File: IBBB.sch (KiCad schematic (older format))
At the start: 11 parts

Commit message: Updates to schematics.  Still very rough
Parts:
- removed C?: 0.1u, symbol C
- removed IC?: AT24CS32-STUM, SOT-23-5, symbol AT24CS32-STUM
- removed R? (x2): 1.5k, 1%, symbol R
- removed R?: 10k, 1%, symbol R
- removed U?: OSD3358, symbol OSD3358
- added C?: 2.2u, symbol C
- added R?: 10k, symbol R
- added SW?: SW_PUSH, symbol SW_PUSH
- added U?: SN74LVC1G07, symbol SN74LVC1G07
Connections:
- net +3V3_B: now also R?.1
- net GND: now also C?.2, SW?.1, U?.3
- net at U?.A10 (WARMRSTN): now also C?.1, R?.2, SW?.2, U?.4 (Y)
- net at U?.A19 (PMIC_OUT_NWAKEUP): now also U?.C5 (EXT_WAKEUP)
- net at U?.A20 (PMIC_OUT_PGOOD): now also U?.B15 (PWRONRSTN), U?.2 (A)
- net at U?.B18 (EXTINTN): now also U?.B19 (PMIC_OUT_NINT)
- net at U?.B20 (PMIC_OUT_LDO_PGOOD): now also U?.B5 (RTC_PWRONRSTN)
- net USB_DC: now reaches U?.Y8 (VIN_USB_Y8)
- net USB_DC: now also U?.Y9 (VIN_USB_Y9)
- net I2C0_SCA renamed USB_UART/I2C0_SDA
- net I2C0_SCL renamed USB_UART/I2C0_SCL
- new net VDD_RTC: U?.5
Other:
- note added: "POWER"
- note added: "RESET"
- note removed: "Board ID"
- moved on the sheet: CON?, D?, R?, SW?, U?A

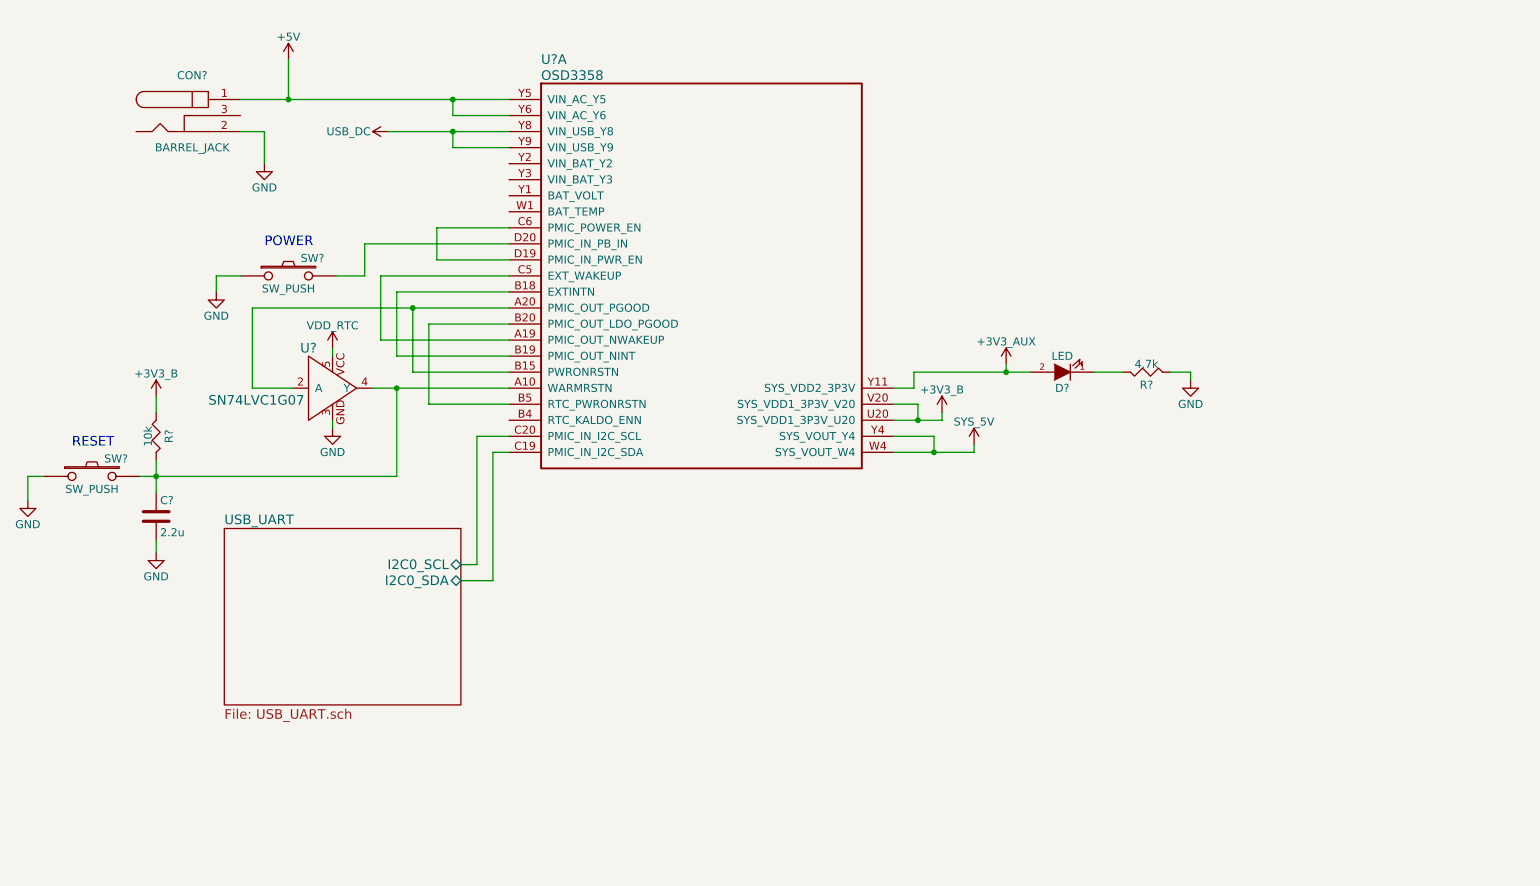
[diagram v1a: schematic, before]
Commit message: Added oscillator and power sheets
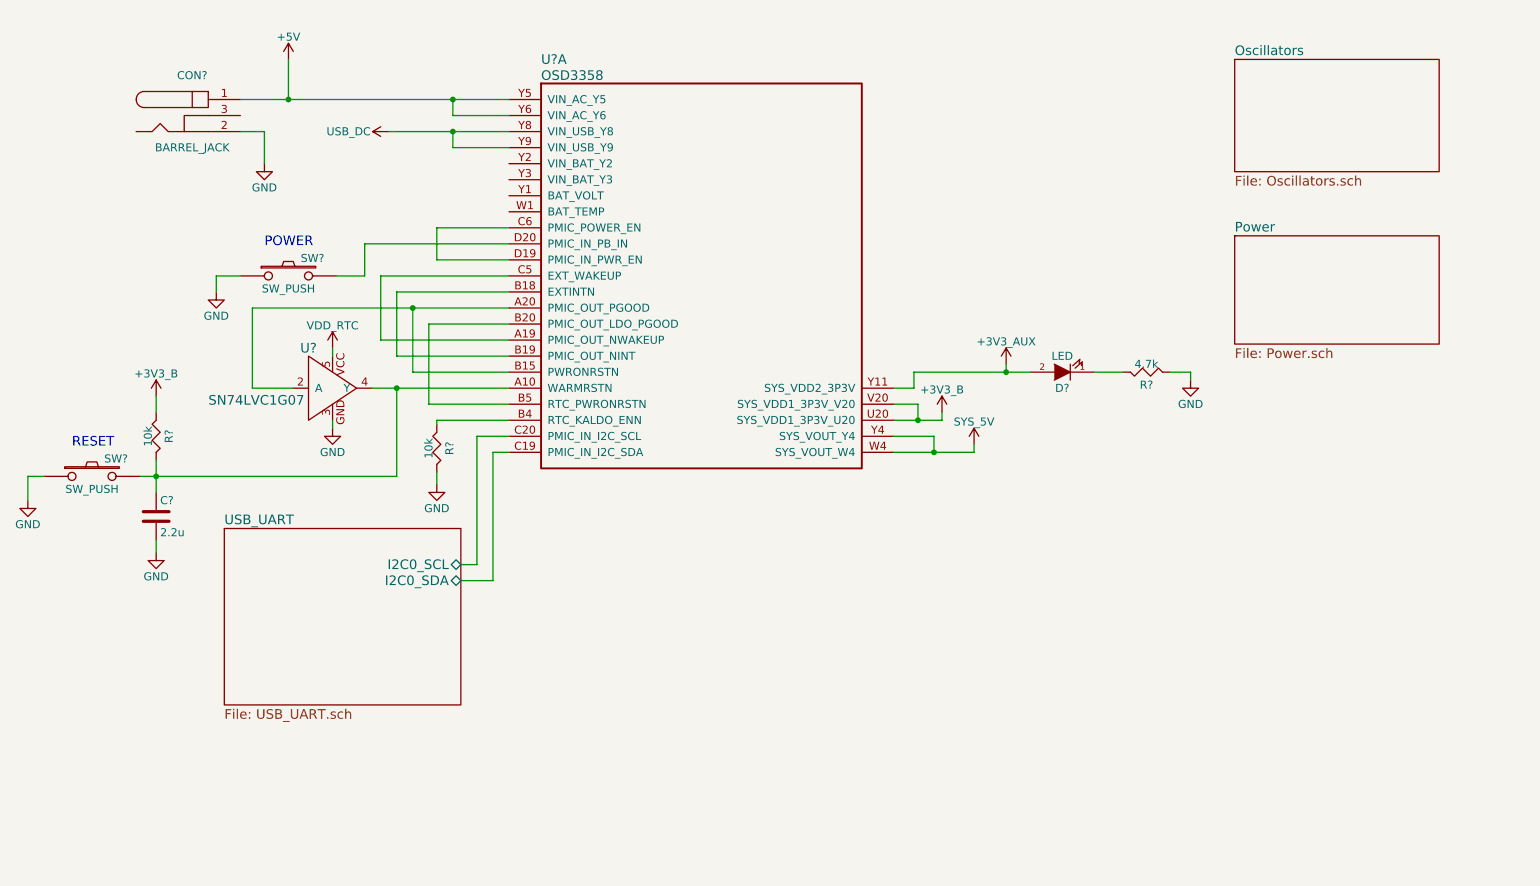
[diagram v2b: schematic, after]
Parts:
- added R?: 10k, symbol R
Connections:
- net GND: now also R?.2
- net at U?.B4 (RTC_KALDO_ENN): now also R?.1
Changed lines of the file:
@@
 $Descr A4 11693 8268
 encoding utf-8
-Sheet 1 2
+Sheet 1 4
 Title "IBBB"
 Date "2016-05-14"
@@
 $EndComp
 Wire Wire Line
-	2325 1200 2625 1200
-Wire Wire Line
-	2625 1200 3650 1200
-Wire Wire Line
-	3650 1200 4000 1200
+	2325 1200 4000 1200
 Wire Wire Line
 	4000 1300 3650 1300
@@
 $EndComp
 Wire Wire Line
-	6400 3400 6650 3400
-Wire Wire Line
-	6650 3400 6900 3400
+	6400 3400 6900 3400
 Wire Wire Line
 	6400 3300 6650 3300
@@
 	6550 3100 6550 3200
 Wire Wire Line
-	6400 3200 6550 3200
-Wire Wire Line
-	6550 3200 6700 3200
+	6400 3200 6700 3200
 Wire Wire Line
 	6700 3200 6700 3150
@@
 	6525 3000 6525 2900
 Wire Wire Line
-	6525 2900 7100 2900
-Wire Wire Line
-	7100 2900 7250 2900
+	6525 2900 7250 2900
 Wire Wire Line
 	7100 2900 7100 2850
@@
 $EndComp
 Wire Wire Line
-	2400 2500 3400 2500
-Wire Wire Line
-	3400 2500 4000 2500
+	2400 2500 4000 2500
 Wire Wire Line
 	3400 2500 3400 2900
@@
 Connection ~ 3400 2500
 Wire Wire Line
-	3150 3000 3300 3000
-Wire Wire Line
-	3300 3000 4000 3000
+	3150 3000 4000 3000
 Wire Wire Line
 	2900 3250 2900 3200
@@
 $EndComp
 Wire Wire Line
-	1800 3450 1800 3550
-Wire Wire Line
-	1800 3550 1800 3650
-Wire Wire Line
-	1700 3550 1800 3550
-Wire Wire Line
-	1800 3550 3300 3550
+	1800 3450 1800 3650
+Wire Wire Line
+	1700 3550 3300 3550
 Connection ~ 1800 3550
 Wire Wire Line
@@
 	3900 4200 3700 4200
 Wire Wire Line
-	3250 1400 3650 1400
-Wire Wire Line
-	3650 1400 4000 1400
+	3250 1400 4000 1400
 Wire Wire Line
 	4000 1500 3650 1500
@@
 	0    -1   -1   0
 $EndComp
+$Sheet
+S 8525 950  1275 700
+U 5738A7C2
+F0 "Oscillators" 60
+F1 "Oscillators.sch" 60
+$EndSheet
+$Sheet
+S 8525 2050 1275 675
+U 5738C205
+F0 "Power" 60
+F1 "Power.sch" 60
+$EndSheet
+$Comp
+L R R?
+U 1 1 5738D8EE
+P 3550 3375
+F 0 "R?" V 3630 3375 50  0000 C CNN
+F 1 "10k" V 3500 3375 50  0000 C CNN
+F 2 "" V 3480 3375 30  0000 C CNN
+F 3 "" H 3550 3375 30  0000 C CNN
+	1    3550 3375
+	1    0    0    -1
+$EndComp
+Wire Wire Line
+	4000 3200 3550 3200
+Wire Wire Line
+	3550 3200 3550 3225
+$Comp
+L GND #PWR?
+U 1 1 5738D9A2
+P 3550 3600
+F 0 "#PWR?" H 3550 3350 50  0001 C CNN
+F 1 "GND" H 3550 3450 50  0000 C CNN
+F 2 "" H 3550 3600 50  0000 C CNN
+F 3 "" H 3550 3600 50  0000 C CNN
+	1    3550 3600
+	1    0    0    -1
+$EndComp
+Wire Wire Line
+	3550 3600 3550 3525
 $EndSCHEMATC

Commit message: Added analog and GPIO sheet
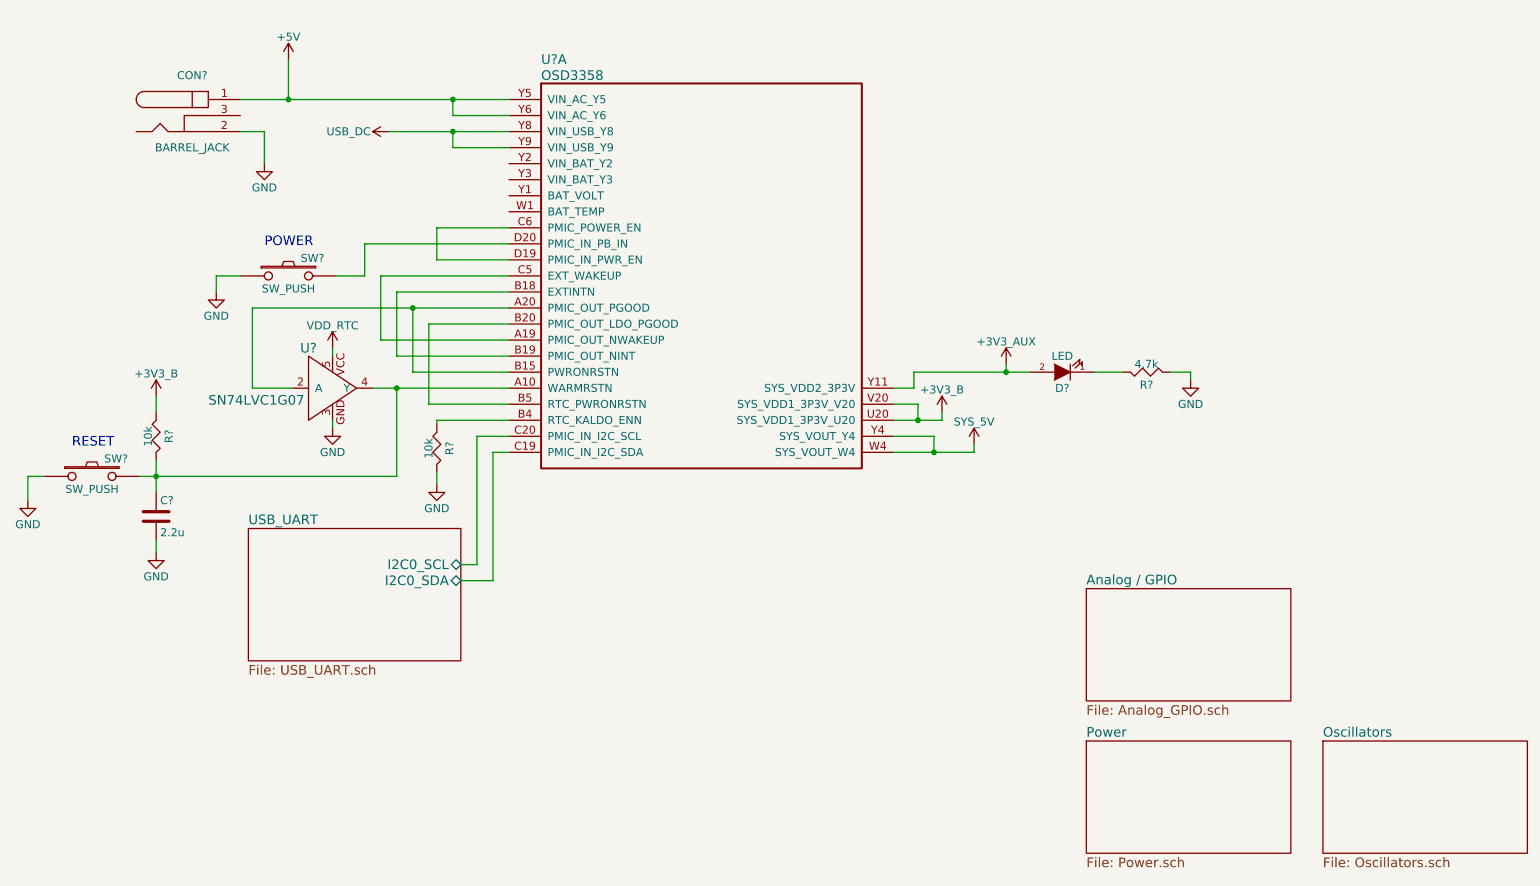
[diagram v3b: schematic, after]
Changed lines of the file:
@@
 $Descr A4 11693 8268
 encoding utf-8
-Sheet 1 4
+Sheet 1 5
 Title "IBBB"
 Date "2016-05-14"
@@
 $EndComp
 $Sheet
-S 2225 3875 1475 1100
+S 2375 3875 1325 825
 U 57381327
 F0 "USB_UART" 60
@@
 $EndComp
 $Sheet
-S 8525 950  1275 700
+S 9075 5200 1275 700
 U 5738A7C2
 F0 "Oscillators" 60
@@
 $EndSheet
 $Sheet
-S 8525 2050 1275 675
+S 7600 5200 1275 700
 U 5738C205
 F0 "Power" 60
@@
 Wire Wire Line
 	3550 3600 3550 3525
+$Sheet
+S 7600 4250 1275 700
+U 5738D4D2
+F0 "Analog / GPIO" 60
+F1 "Analog_GPIO.sch" 60
+$EndSheet
 $EndSCHEMATC

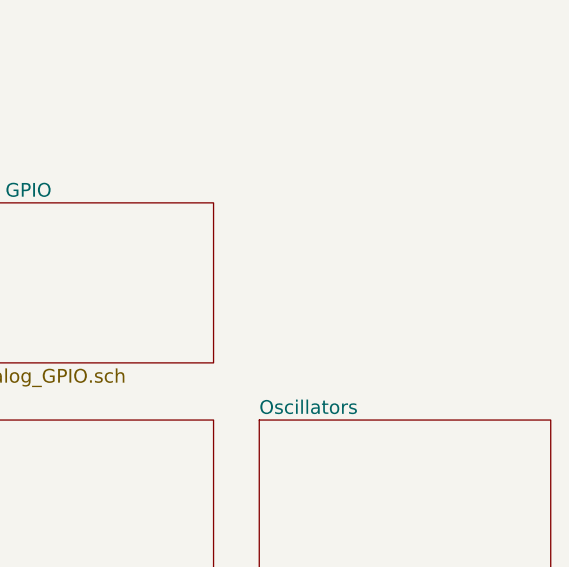
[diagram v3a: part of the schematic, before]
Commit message: Added Sysboot configuration, user LEDs, updated README
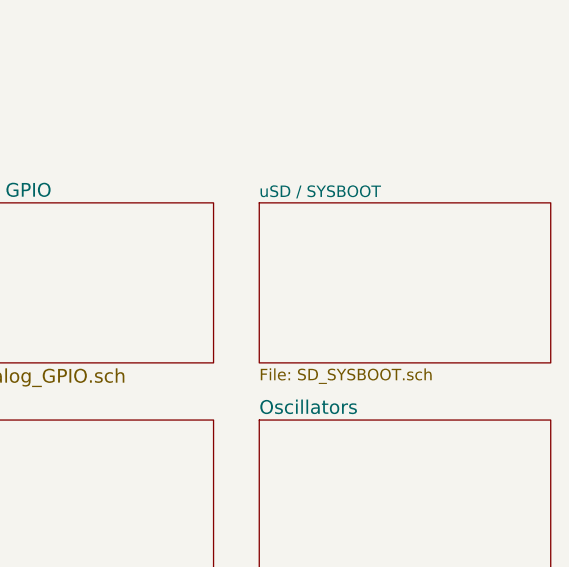
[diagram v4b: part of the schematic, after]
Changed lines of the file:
@@
 $Descr A4 11693 8268
 encoding utf-8
-Sheet 1 5
+Sheet 1 6
 Title "IBBB"
 Date "2016-05-14"
@@
 F1 "Analog_GPIO.sch" 60
 $EndSheet
+$Sheet
+S 9075 4250 1275 700
+U 573A65DA
+F0 "uSD / SYSBOOT" 50
+F1 "SD_SYSBOOT.sch" 50
+$EndSheet
 $EndSCHEMATC
